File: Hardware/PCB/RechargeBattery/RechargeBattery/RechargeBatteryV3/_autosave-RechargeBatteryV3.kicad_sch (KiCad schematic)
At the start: 19 parts, among them IC1 BQ25895MRTWT, J1 USB_C_Receptacle_USB2.0_16P

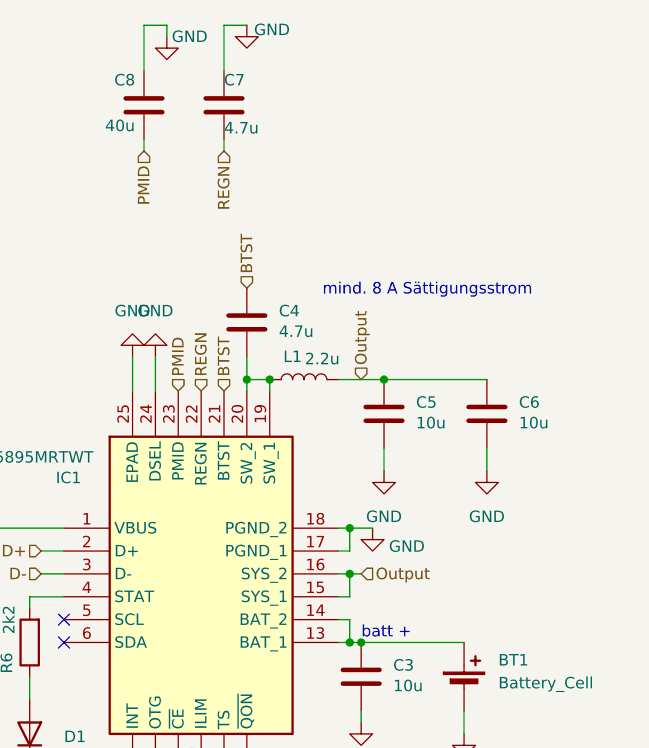
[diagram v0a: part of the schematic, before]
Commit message: batterie recharing system V3 with BQ25895M chip
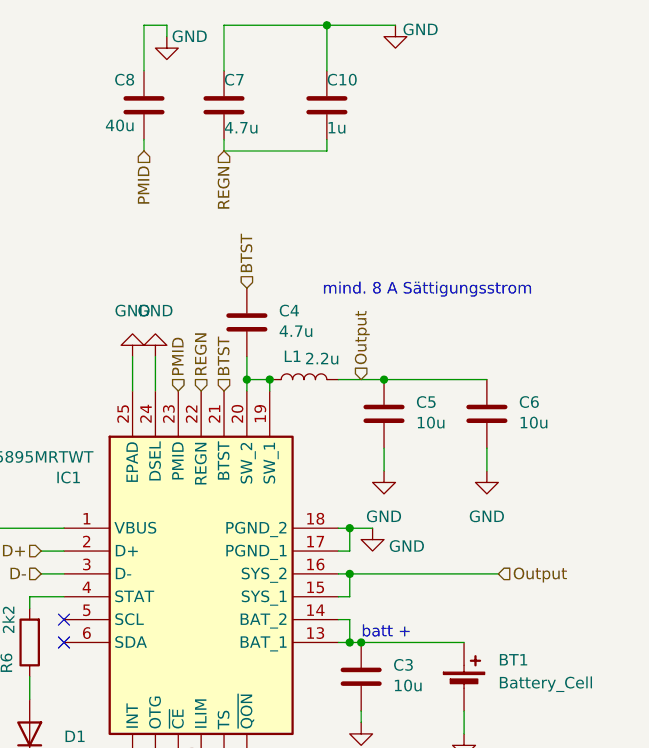
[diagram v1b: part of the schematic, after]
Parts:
- added C10: 1u, Capacitor_SMD:C_0603_1608Metric, symbol Device:C
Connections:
- net GND: now also C10.1
- net REGN: now also C10.2
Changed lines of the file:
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@@
+		(color 0 0 0 0)
+	)
+	(junction
+		(at 228.6 21.59)
+		(diameter 0)
 		(color 0 0 0 0)
 	)
@@
 	(wire
 		(pts
-			(xy 219.71 21.59) (xy 217.17 21.59)
+			(xy 217.17 21.59) (xy 228.6 21.59)
 		)
 		(stroke
@@
 	(wire
 		(pts
+			(xy 228.6 21.59) (xy 228.6 26.67)
+		)
+		(stroke
+			(width 0)
+			(type default)
+		)
+	)
+	(wire
+		(pts
 			(xy 231.14 77.47) (xy 229.87 77.47)
 		)
@@
 	(wire
 		(pts
+			(xy 228.6 21.59) (xy 236.22 21.59)
+		)
+		(stroke
+			(width 0)
+			(type default)
+		)
+	)
+	(wire
+		(pts
 			(xy 196.85 80.01) (xy 199.39 80.01)
 		)
@@
 	(wire
 		(pts
-			(xy 231.14 82.55) (xy 232.41 82.55)
+			(xy 231.14 82.55) (xy 247.65 82.55)
 		)
 		(stroke
@@
 	(wire
 		(pts
+			(xy 217.17 35.56) (xy 228.6 35.56)
+		)
+		(stroke
+			(width 0)
+			(type default)
+		)
+	)
+	(wire
+		(pts
 			(xy 229.87 80.01) (xy 231.14 80.01)
 		)
@@
 		(pts
 			(xy 231.14 77.47) (xy 233.68 77.47)
+		)
+		(stroke
+			(width 0)
+			(type default)
+		)
+	)
+	(wire
+		(pts
+			(xy 228.6 35.56) (xy 228.6 34.29)
 		)
 		(stroke
@@
 	(hierarchical_label "Output"
 		(shape input)
-		(at 232.41 82.55 0)
+		(at 247.65 82.55 0)
 		(effects
 			(font
@@
 	)
 	(symbol
+		(lib_id "Device:C")
+		(at 228.6 30.48 0)
+		(unit 1)
+		(exclude_from_sim no)
+		(in_bom yes)
+		(on_board yes)
+		(dnp no)
+		(property "Reference" "C10"
+			(at 228.6 27.686 0)
+			(effects
+				(font
+					(size 1.27 1.27)
+				)
+				(justify left)
+			)
+		)
+		(property "Value" "1u"
+			(at 228.6 33.02 0)
+			(effects
+				(font
+					(size 1.27 1.27)
+				)
+				(justify left)
+			)
+		)
+		(property "Footprint" "Capacitor_SMD:C_0603_1608Metric"
+			(at 229.5652 34.29 0)
+			(effects
+				(font
+					(size 1.27 1.27)
+				)
+				(hide yes)
+			)
+		)
+		(property "Datasheet" "~"
+			(at 228.6 30.48 0)
+			(effects
+				(font
+					(size 1.27 1.27)
+				)
+				(hide yes)
+			)
+		)
+		(property "Description" "Unpolarized capacitor"
+			(at 228.6 30.48 0)
+			(effects
+				(font
+					(size 1.27 1.27)
+				)
+				(hide yes)
+			)
+		)
+		(pin "1"
+		)
+		(pin "2"
+		)
+		(instances
+			(project "RechargeBatteryV3"
+				(path "/3c1b30d6-d4e4-4579-9023-d07a7c247741"
+					(reference "C10")
+					(unit 1)
+				)
+			)
+		)
+	)
+	(symbol
 		(lib_id "power:GND")
 		(at 99.06 78.74 90)
@@
 	(symbol
 		(lib_id "power:GND")
-		(at 219.71 21.59 0)
+		(at 236.22 21.59 0)
 		(unit 1)
 		(exclude_from_sim no)
@@
 		(dnp no)
 		(property "Reference" "#PWR011"
-			(at 219.71 27.94 0)
+			(at 236.22 27.94 0)
 			(effects
 				(font
@@
 		)
 		(property "Value" "GND"
-			(at 222.504 22.098 0)
+			(at 239.014 22.098 0)
 			(effects
 				(font
@@
 		)
 		(property "Footprint" ""
-			(at 219.71 21.59 0)
+			(at 236.22 21.59 0)
 			(effects
 				(font
@@
 		)
 		(property "Datasheet" ""
-			(at 219.71 21.59 0)
+			(at 236.22 21.59 0)
 			(effects
 				(font
@@
 		)
 		(property "Description" "Power symbol creates a global label with name \"GND\" , ground"
-			(at 219.71 21.59 0)
-			(effects
-				(font
+			(at 236.22 21.59 0)
+			(effects
+				(font
